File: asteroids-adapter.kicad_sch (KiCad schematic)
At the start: 15 parts, among them J1 Asteroids PCB connector, J2 Asteroids harness connector, U1 TL074

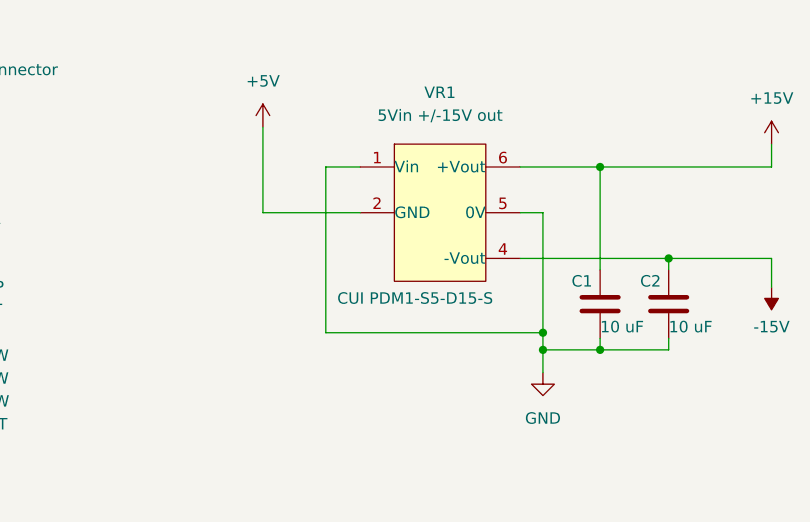
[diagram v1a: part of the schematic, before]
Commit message: Power and GND to DC-DC converter were swapped
Fixed by swapping the power and ground connections to pins 1 and 2 of
the DC-DC converter.
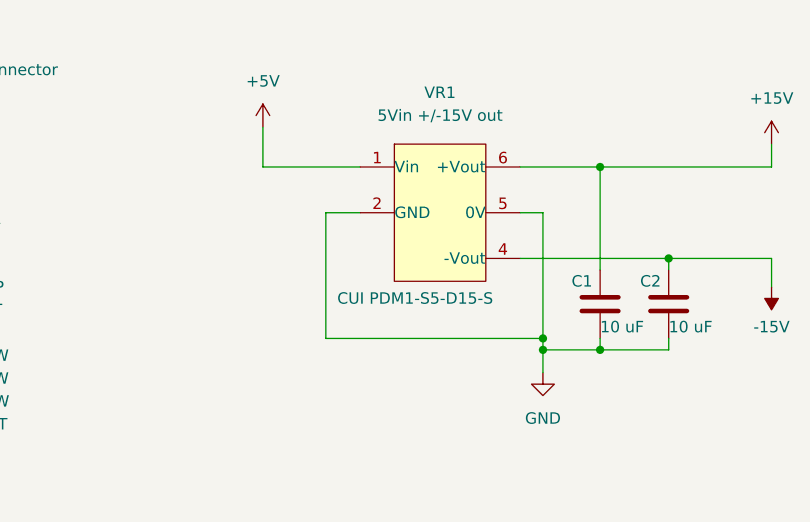
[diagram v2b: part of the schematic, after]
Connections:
- net +5V: now also VR1.1 (Vin); no longer VR1.2 (GND)
- net GND: now also VR1.2 (GND); no longer VR1.1 (Vin)
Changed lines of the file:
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@@
     (rev "1.2")
   )
-  (junction (at 163.195 48.26) (diameter 0) (color 0 0 0 0)
-  )
   (junction (at 62.23 72.39) (diameter 0) (color 0 0 0 0)
   )
@@
   )
   (junction (at 196.85 85.725) (diameter 0) (color 0 0 0 0)
+  )
+  (junction (at 163.195 48.895) (diameter 0) (color 0 0 0 0)
   )
   (junction (at 191.77 132.715) (diameter 0) (color 0 0 0 0)
@@
     (stroke (width 0) (type default) (color 0 0 0 0))
   )
+  (wire (pts (xy 139.065 34.925) (xy 139.065 48.895))
+    (stroke (width 0) (type default) (color 0 0 0 0))
+  )
   (wire (pts (xy 82.55 50.8) (xy 85.09 50.8))
     (stroke (width 0) (type default) (color 0 0 0 0))
@@
     (stroke (width 0) (type default) (color 0 0 0 0))
   )
-  (wire (pts (xy 139.065 48.26) (xy 163.195 48.26))
-    (stroke (width 0) (type default) (color 0 0 0 0))
-  )
   (wire (pts (xy 82.55 106.68) (xy 85.09 106.68))
     (stroke (width 0) (type default) (color 0 0 0 0))
@@
     (stroke (width 0) (type default) (color 0 0 0 0))
   )
-  (wire (pts (xy 142.875 34.925) (xy 132.08 34.925))
-    (stroke (width 0) (type default) (color 0 0 0 0))
-  )
   (wire (pts (xy 163.195 95.885) (xy 160.02 95.885))
     (stroke (width 0) (type default) (color 0 0 0 0))
@@
     (stroke (width 0) (type default) (color 0 0 0 0))
   )
-  (wire (pts (xy 163.195 34.925) (xy 163.195 48.26))
-    (stroke (width 0) (type default) (color 0 0 0 0))
-  )
   (wire (pts (xy 120.65 158.115) (xy 120.65 159.385))
     (stroke (width 0) (type default) (color 0 0 0 0))
@@
     (stroke (width 0) (type default) (color 0 0 0 0))
   )
-  (wire (pts (xy 142.875 29.845) (xy 139.065 29.845))
+  (wire (pts (xy 132.08 29.845) (xy 142.875 29.845))
     (stroke (width 0) (type default) (color 0 0 0 0))
   )
@@
     (stroke (width 0) (type default) (color 0 0 0 0))
   )
+  (wire (pts (xy 142.875 34.925) (xy 139.065 34.925))
+    (stroke (width 0) (type default) (color 0 0 0 0))
+  )
   (wire (pts (xy 113.03 169.545) (xy 113.03 184.785))
     (stroke (width 0) (type default) (color 0 0 0 0))
@@
     (stroke (width 0) (type default) (color 0 0 0 0))
   )
+  (wire (pts (xy 163.195 48.895) (xy 163.195 50.165))
+    (stroke (width 0) (type default) (color 0 0 0 0))
+  )
   (wire (pts (xy 160.655 40.005) (xy 177.165 40.005))
     (stroke (width 0) (type default) (color 0 0 0 0))
@@
     (stroke (width 0) (type default) (color 0 0 0 0))
   )
-  (wire (pts (xy 139.065 29.845) (xy 139.065 48.26))
-    (stroke (width 0) (type default) (color 0 0 0 0))
-  )
   (wire (pts (xy 174.625 83.82) (xy 184.785 83.82))
     (stroke (width 0) (type default) (color 0 0 0 0))
@@
     (stroke (width 0) (type default) (color 0 0 0 0))
   )
-  (wire (pts (xy 132.08 34.925) (xy 132.08 25.4))
-    (stroke (width 0) (type default) (color 0 0 0 0))
-  )
   (wire (pts (xy 46.99 53.34) (xy 49.53 53.34))
     (stroke (width 0) (type default) (color 0 0 0 0))
@@
     (stroke (width 0) (type default) (color 0 0 0 0))
   )
+  (wire (pts (xy 139.065 48.895) (xy 163.195 48.895))
+    (stroke (width 0) (type default) (color 0 0 0 0))
+  )
   (wire (pts (xy 46.99 121.92) (xy 49.53 121.92))
     (stroke (width 0) (type default) (color 0 0 0 0))
@@
     (stroke (width 0) (type default) (color 0 0 0 0))
   )
+  (wire (pts (xy 132.08 25.4) (xy 132.08 29.845))
+    (stroke (width 0) (type default) (color 0 0 0 0))
+  )
   (wire (pts (xy 169.545 48.895) (xy 169.545 50.165))
     (stroke (width 0) (type default) (color 0 0 0 0))
@@
     (stroke (width 0) (type default) (color 0 0 0 0))
   )
-  (wire (pts (xy 163.195 48.26) (xy 163.195 50.165))
-    (stroke (width 0) (type default) (color 0 0 0 0))
-  )
+  (wire (pts (xy 163.195 34.925) (xy 163.195 48.895))
+    (stroke (width 0) (type default) (color 0 0 0 0))
+  )

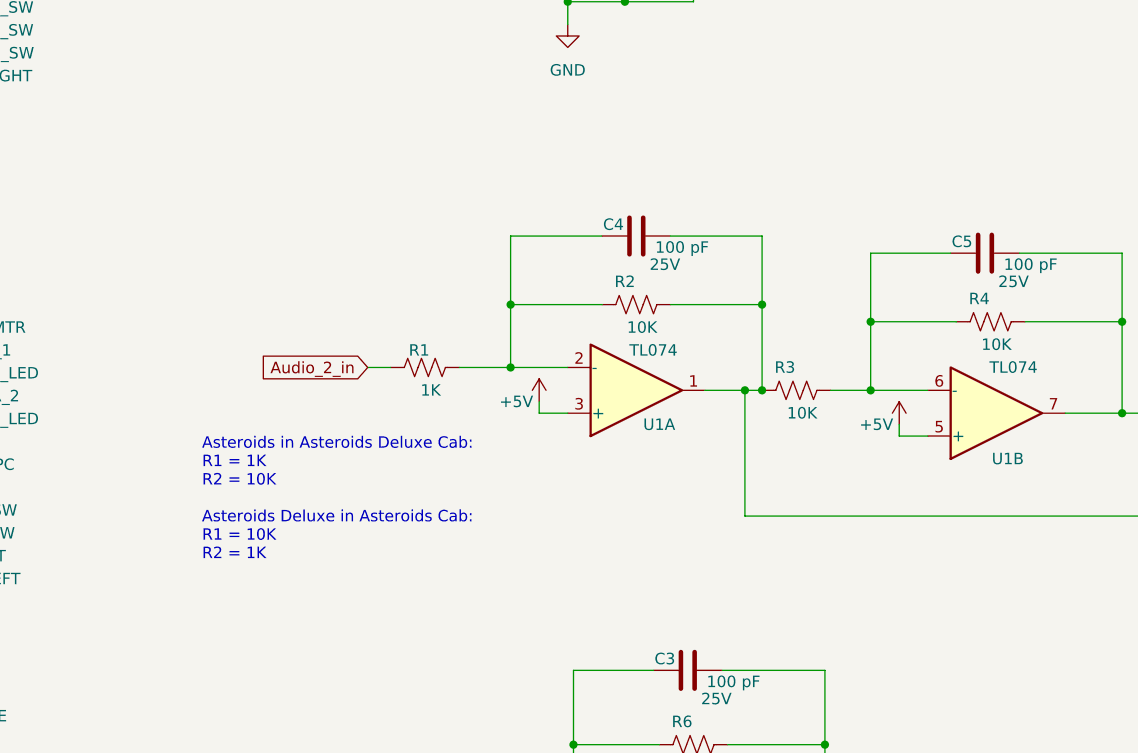
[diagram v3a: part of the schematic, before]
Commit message: Add bypass to 5V op-amp reference
- Added 10 uf cap at (+) input of both audio inverter op amps, to reduce
noise.
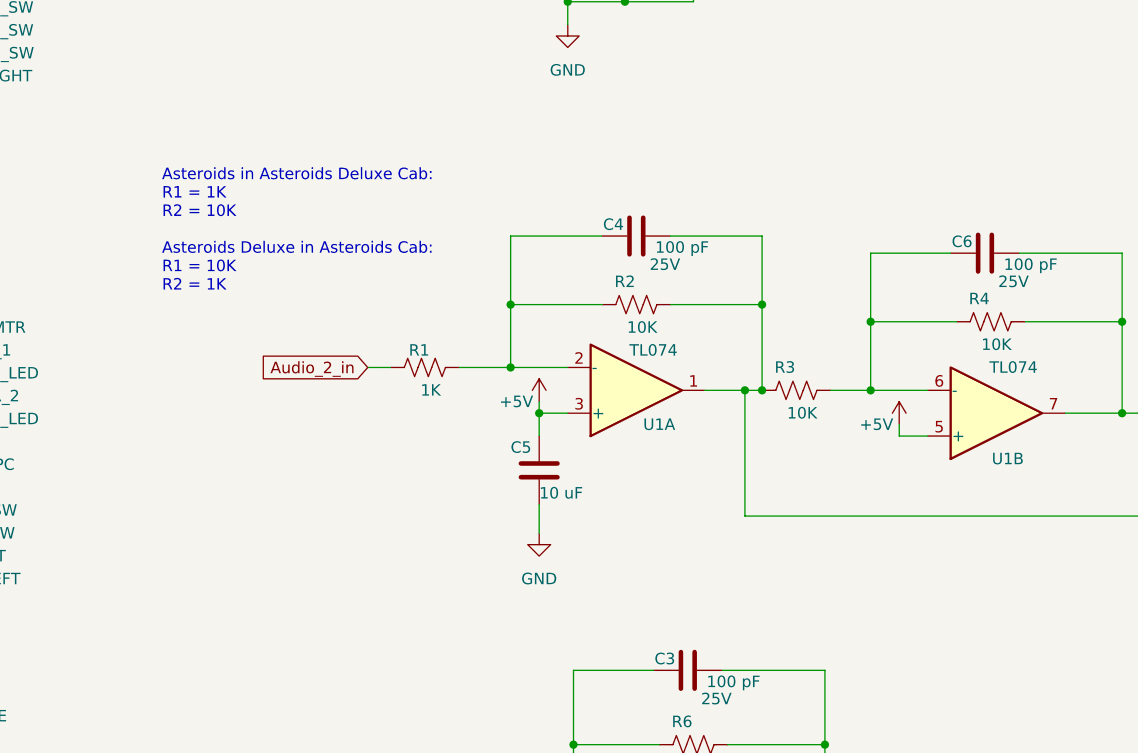
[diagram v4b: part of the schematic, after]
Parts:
- added C5: Kemet 10 uF 25V MLCC TH, Capacitor_THT:C_Disc_D3.0mm_W1.6mm_P2.50mm, symbol ast-adapter:Kemet 10 uF 25V MLCC TH
- renumbered C5 to C6
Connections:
- net +5V: now also C5.2
- net GND: now also C5.1
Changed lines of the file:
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@@
   (junction (at 224.79 85.725) (diameter 0) (color 0 0 0 0)
+  )
+  (junction (at 160.02 95.885) (diameter 0) (color 0 0 0 0)
   )
   (junction (at 191.77 142.875) (diameter 0) (color 0 0 0 0)
@@
     (stroke (width 0) (type default) (color 0 0 0 0))
   )
+  (wire (pts (xy 160.02 95.885) (xy 160.02 98.425))
+    (stroke (width 0) (type default) (color 0 0 0 0))
+  )
   (wire (pts (xy 82.55 109.22) (xy 85.09 109.22))
     (stroke (width 0) (type default) (color 0 0 0 0))
@@
     (stroke (width 0) (type default) (color 0 0 0 0))
   )
+  (wire (pts (xy 160.02 106.045) (xy 160.02 109.22))
+    (stroke (width 0) (type default) (color 0 0 0 0))
+  )
   (wire (pts (xy 167.005 145.415) (xy 167.005 147.32))
     (stroke (width 0) (type default) (color 0 0 0 0))
@@
   )
   (text "Asteroids in Asteroids Deluxe Cab:\nR1 = 1K\nR2 = 10K\n\nAsteroids Deluxe in Asteroids Cab:\nR1 = 10K\nR2 = 1K"
-    (at 122.555 112.395 0)
+    (at 118.11 82.55 0)
     (effects (font (size 1.27 1.27)) (justify left bottom))
   )
@@
     )
   )
+  (symbol (lib_id "power:GND") (at 160.02 109.22 0) (unit 1)
+    (in_bom yes) (on_board yes) (fields_autoplaced)
+    (property "Reference" "#PWR01" (id 0) (at 160.02 115.57 0)
+      (effects (font (size 1.27 1.27)) hide)
+    )
+    (property "Value" "GND" (id 1) (at 160.02 114.3 0))
+    (property "Footprint" "" (id 2) (at 160.02 109.22 0)
+      (effects (font (size 1.27 1.27)) hide)
+    )
+    (property "Datasheet" "" (id 3) (at 160.02 109.22 0)
+      (effects (font (size 1.27 1.27)) hide)
+    )
+    (pin "1")
+  )
   (symbol (lib_id "power:GND") (at 163.195 52.705 0) (unit 1)
     (in_bom yes) (on_board yes) (fields_autoplaced)
@@
   (symbol (lib_id "ast-adapter: Kemet MLCC 100 pF 5% 25V TH") (at 209.55 78.105 0) (unit 1)
     (in_bom yes) (on_board yes)
-    (property "Reference" "C5" (id 0) (at 207.01 76.835 0))
+    (property "Reference" "C6" (id 0) (at 207.01 76.835 0))
     (property "Value" " Kemet MLCC 100 pF 5% 25V TH" (id 1) (at 152.4 110.236 0)
       (effects (font (size 1.27 1.27)) (justify left) hide)
@@
     )
     (property "Class" "If applicable" (id 26) (at 106.553 146.939 0)
+      (effects (font (size 1.27 1.27)) hide)
+    )
+    (pin "1")
+    (pin "2")
+  )
+  (symbol (lib_id "ast-adapter:Kemet 10 uF 25V MLCC TH") (at 160.02 102.235 90) (unit 1)
+    (in_bom yes) (on_board yes)
+    (property "Reference" "C5" (id 0) (at 156.845 99.695 90)
+      (effects (font (size 1.27 1.27)) (justify right))
+    )
+    (property "Value" "Kemet 10 uF 25V MLCC TH" (id 1) (at 194.818 130.175 0)
+      (effects (font (size 1.27 1.27)) (justify left) hide)
+    )
+    (property "Footprint" "Capacitor_THT:C_Disc_D3.0mm_W1.6mm_P2.50mm" (id 2) (at 175.26 126.365 0)
+      (effects (font (size 1.27 1.27)) hide)
+    )
+    (property "Datasheet" "https://connect.kemet.com:7667/gateway/IntelliData-ComponentDocumentation/1.0/download/datasheet/C320C475K3N5TA91707301.pdf" (id 3) (at 189.484 128.397 0)
+      (effects (font (size 1.27 1.27)) hide)
+    )
+    (property "Component Value" "10 uF" (id 4) (at 160.02 104.775 90)
+      (effects (font (size 1.27 1.27)) (justify right))
+    )
+    (property "Tolerance" "If applicable" (id 5) (at 199.644 124.333 0)
+      (effects (font (size 1.27 1.27)) hide)
+    )
+    (property "Manufacturer" "Kemet" (id 6) (at 178.308 128.397 0)
+      (effects (font (size 1.27 1.27)) hide)
+    )
+    (property "Manufacturer Link" "https://www.kemet.com/en/us/search.html?q=+C320C475K3N5TA91707301" (id 7) (at 184.912 125.603 0)
+      (effects (font (size 1.27 1.27)) hide)
+    )
+    (property "RoHS Document Link" "https://www.mouser.com/Search/RoHSCompliant?qs=FDDWrLyJ7y%2fieItPZb13LQ%3d%3d" (id 8) (at 224.79 125.349 0)
+      (effects (font (size 1.27 1.27)) hide)
+    )
+    (property "Manufacturer PN" " C320C475K3N5TA91707301 " (id 9) (at 181.864 126.111 0)
+      (effects (font (size 1.27 1.27)) hide)
+    )
+    (property "RoHS" "Yes" (id 10) (at 221.996 128.651 0)
+      (effects (font (size 1.27 1.27)) hide)
+    )
+    (property "Allow Substitution" "Yes" (id 11) (at 227.838 128.905 0)
+      (effects (font (size 1.27 1.27)) hide)
+    )
+    (property "Fitted" "Yes" (id 12) (at 232.664 127.889 0)
+      (effects (font (size 1.27 1.27)) hide)
+    )
+    (property "Tracking" "No" (id 13) (at 230.124 128.397 0)
+      (effects (font (size 1.27 1.27)) hide)
+    )
+    (property "BOM Comment" "" (id 14) (at 160.02 102.235 0)
+      (effects (font (size 1.27 1.27)) hide)
+    )
+    (property "Component Type" "Capacitor" (id 15) (at 196.85 106.807 0)
+      (effects (font (size 1.27 1.27)) hide)
+    )
+    (property "Package Type" "Radial" (id 16) (at 172.085 129.54 0)
+      (effects (font (size 1.27 1.27)) hide)
+    )
+    (property "Package Variant" "" (id 17) (at 160.02 102.235 0)
+      (effects (font (size 1.27 1.27)) hide)
+    )
+    (property "Number of Pins" "If applicable" (id 18) (at 202.184 124.333 0)
+      (effects (font (size 1.27 1.27)) hide)
+    )
+    (property "Temp (Storage)" "If applicable" (id 19) (at 204.216 124.333 0)
+      (effects (font (size 1.27 1.27)) hide)
+    )
+    (property "Temp (Operating)" "If applicable" (id 20) (at 206.756 124.079 0)
+      (effects (font (size 1.27 1.27)) hide)
+    )
+    (property "Temp (Soldering)" "If applicable" (id 21) (at 209.55 124.079 0)
+      (effects (font (size 1.27 1.27)) hide)
+    )
+    (property "Temp Coeff." "If applicable" (id 22) (at 212.09 124.079 0)
+      (effects (font (size 1.27 1.27)) hide)
+    )
+    (property "Power Rating" "If applicable" (id 23) (at 214.63 124.079 0)
+      (effects (font (size 1.27 1.27)) hide)
+    )
+    (property "Material" "If applicable" (id 24) (at 216.916 124.079 0)
+      (effects (font (size 1.27 1.27)) hide)
+    )
+    (property "Class" "If applicable" (id 25) (at 219.202 124.079 0)
+      (effects (font (size 1.27 1.27)) hide)
+    )
+    (property "Standards Version" "1.1" (id 26) (at 235.712 127.889 0)
       (effects (font (size 1.27 1.27)) hide)
     )
@@
   )
   (symbol_instances
+    (path "/13b51276-0fe7-4c29-b159-a8a4782eb7c4"
+      (reference "#PWR01") (unit 1) (value "GND") (footprint "")
+    )
     (path "/7374c83c-84e1-41d7-9bd3-720fed686bcc"
       (reference "#PWR0101") (unit 1) (value "+5V") (footprint "")
@@
       (reference "C4") (unit 1) (value " Kemet MLCC 100 pF 5% 25V TH") (footprint "Capacitor_THT:C_Disc_D3.0mm_W1.6mm_P2.50mm")
     )
+    (path "/61197094-22b2-43e4-a0d8-a7b95d10d938"
+      (reference "C5") (unit 1) (value "Kemet 10 uF 25V MLCC TH") (footprint "Capacitor_THT:C_Disc_D3.0mm_W1.6mm_P2.50mm")
+    )
     (path "/291c911a-57fb-4917-a04a-4a0926417f3f"
-      (reference "C5") (unit 1) (value " Kemet MLCC 100 pF 5% 25V TH") (footprint "Capacitor_THT:C_Disc_D3.0mm_W1.6mm_P2.50mm")
+      (reference "C6") (unit 1) (value " Kemet MLCC 100 pF 5% 25V TH") (footprint "Capacitor_THT:C_Disc_D3.0mm_W1.6mm_P2.50mm")
     )
     (path "/c37cb6c3-6fec-4395-b191-aee0441c0811"
